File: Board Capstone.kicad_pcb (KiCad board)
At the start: 2 copper layers, 128 x 50 mm, 40 parts, among them IC201 LM2678SX-5.0, J101 Power, J102 Conn_JetsonNano, J103 Status_LED, J104 Warning_LED, J401 Haptics_1, J402 Haptics_2, SW101 SW_Pairing, U101 SN74LV1T125DBV, U102 SN74LV1T125DBV, U301 ICM-20948, U302 PCA9306, U303 TLV740P, U401 PCA9540BD_112, U402 DRV2605LDGS, U403 DRV2605LDGS

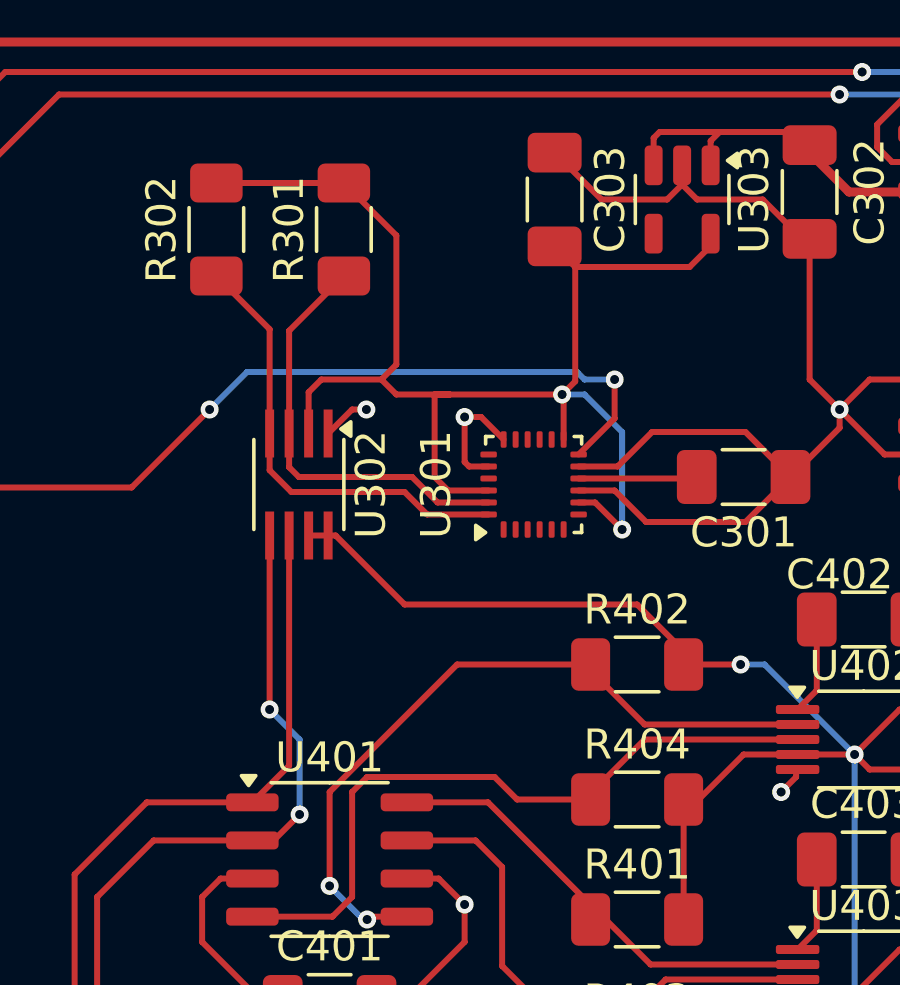
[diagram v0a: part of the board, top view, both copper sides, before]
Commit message: rev 1.1 change footprint
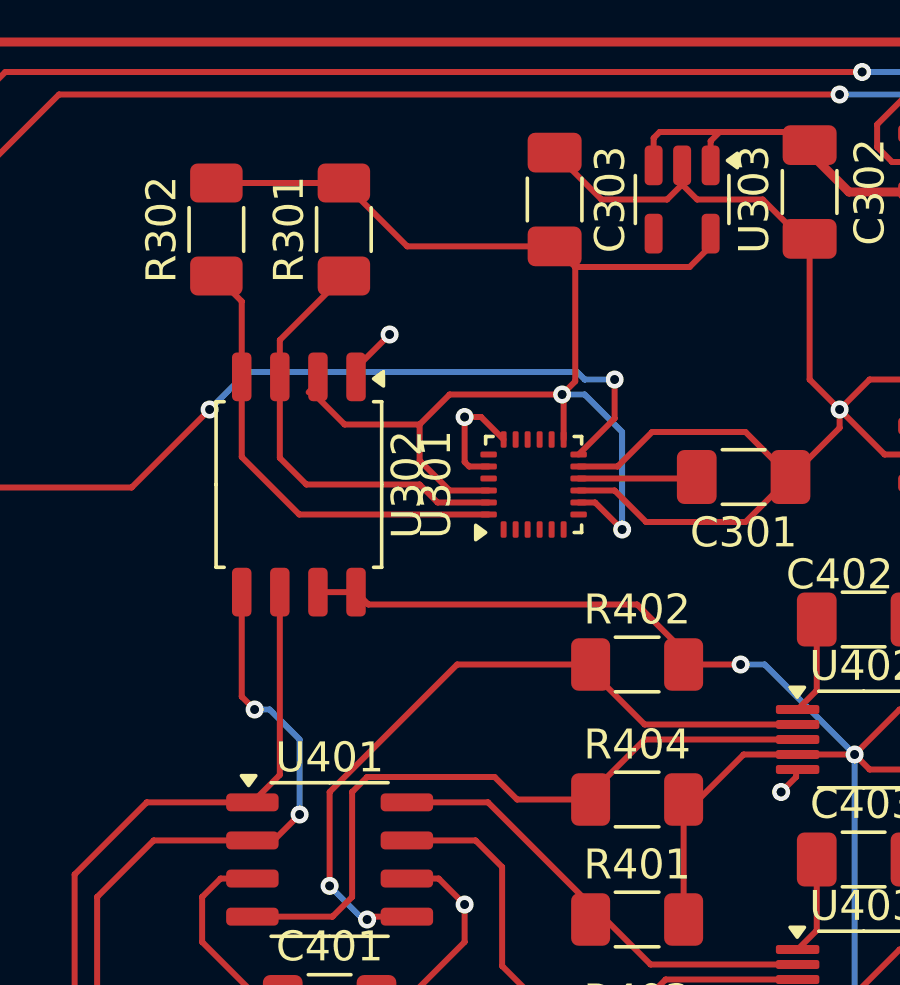
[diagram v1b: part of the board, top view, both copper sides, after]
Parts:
- U302: footprint Package_SO:SSOP-8_2.95x2.8mm_P0.65mm -> Package_SO:SOIC-8_5.3x5.3mm_P1.27mm
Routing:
- net /I2C_SLC: track 74.5 -> 72.5 mm
- net /I2C_SDA: track 80.5 -> 79.3 mm
- net +3.3V: track 163.3 -> 162.2 mm
- net IMU_VDDIO: track 47.3 -> 46.4 mm

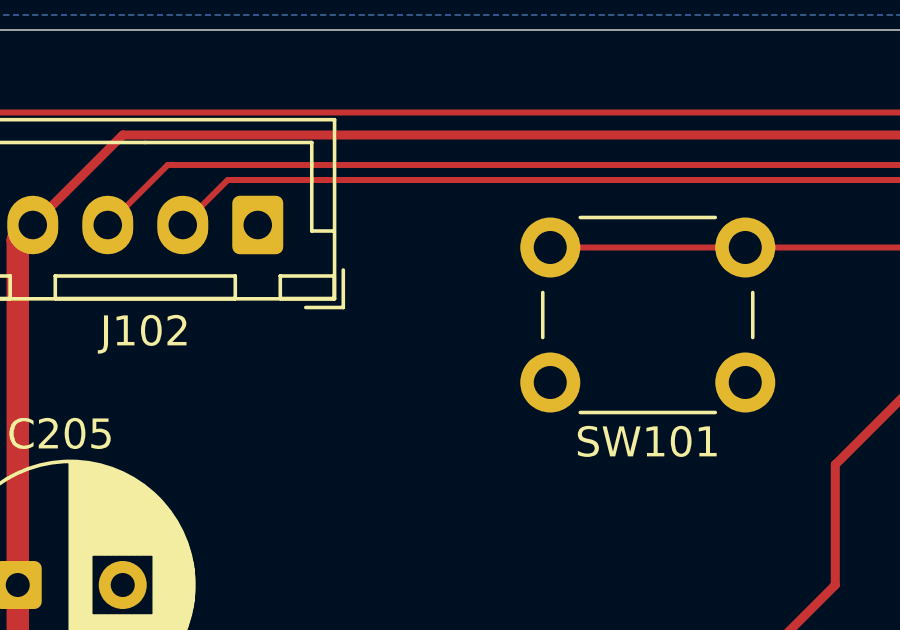
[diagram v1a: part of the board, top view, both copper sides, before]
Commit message: rev 1.1.1 Added decoupling cap to push button
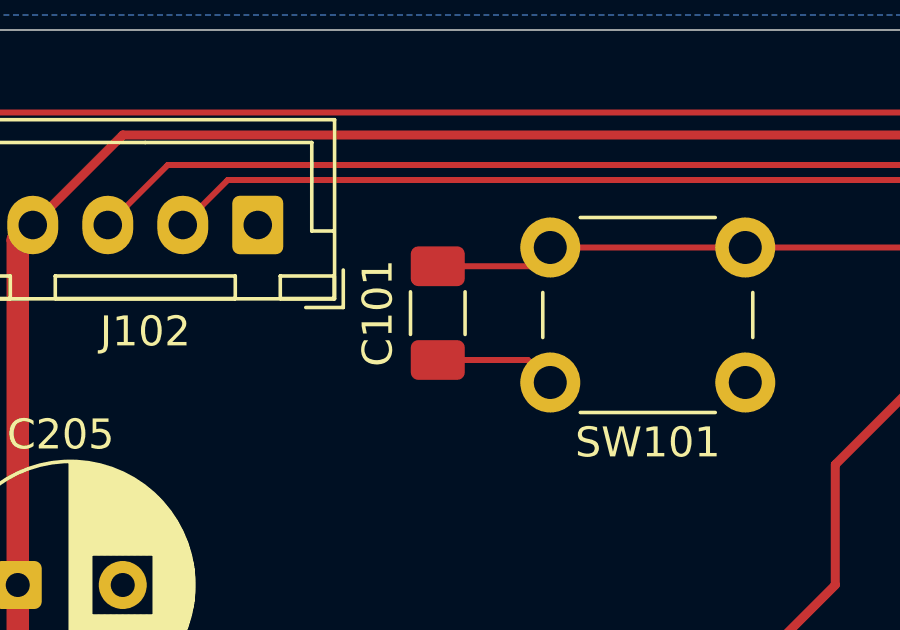
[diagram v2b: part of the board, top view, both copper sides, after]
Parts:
- added C101: 0.1uF, Capacitor_SMD:C_1206_3216Metric_Pad1.33x1.80mm_HandSolder, F.Cu at (99.0, 58.9)
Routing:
- net GND: track 113.0 -> 117.6 mm
- net Net-(A101-D13/SCK): track 14.1 -> 18.6 mm
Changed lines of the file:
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@@
 		)
 	)
+	(footprint "Capacitor_SMD:C_1206_3216Metric_Pad1.33x1.80mm_HandSolder"
+		(layer "F.Cu")
+		(at 99 58.9375 -90)
+		(descr "Capacitor SMD 1206 (3216 Metric), square (rectangular) end terminal, IPC-7351 nominal with elongated pad for handsoldering. (Body size source: IPC-SM-782 page 76, https://www.pcb-3d.com/wordpress/wp-content/uploads/ipc-sm-782a_amendment_1_and_2.pdf), generated with kicad-footprint-generator")
+		(tags "capacitor handsolder")
+		(property "Reference" "C101"
+			(at 0 2 90)
+			(layer "F.SilkS")
+			(effects
+				(font
+					(size 1 1)
+					(thickness 0.15)
+				)
+			)
+		)
+		(property "Value" "0.1uF"
+			(at 0 1.85 90)
+			(layer "F.Fab")
+			(effects
+				(font
+					(size 1 1)
+					(thickness 0.15)
+				)
+			)
+		)
+		(property "Datasheet" ""
+			(at 0 0 90)
+			(layer "F.Fab")
+			(hide yes)
+			(effects
+				(font
+					(size 1.27 1.27)
+					(thickness 0.15)
+				)
+			)
+		)
+		(property "Description" "Unpolarized capacitor, small symbol"
+			(at 0 0 90)
+			(layer "F.Fab")
+			(hide yes)
+			(effects
+				(font
+					(size 1.27 1.27)
+					(thickness 0.15)
+				)
+			)
+		)
+		(property ki_fp_filters "C_*")
+		(sheetname "/")
+		(sheetfile "Board Capstone.kicad_sch")
+		(attr smd)
+		(fp_line
+			(start -0.711252 0.91)
+			(end 0.711252 0.91)
+			(stroke
+				(width 0.12)
+				(type solid)
+			)
+			(layer "F.SilkS")
+		)
+		(fp_line
+			(start -0.711252 -0.91)
+			(end 0.711252 -0.91)
+			(stroke
+				(width 0.12)
+				(type solid)
+			)
+			(layer "F.SilkS")
+		)
+		(fp_line
+			(start -2.48 1.15)
+			(end -2.48 -1.15)
+			(stroke
+				(width 0.05)
+				(type solid)
+			)
+			(layer "F.CrtYd")
+		)
+		(fp_line
+			(start 2.48 1.15)
+			(end -2.48 1.15)
+			(stroke
+				(width 0.05)
+				(type solid)
+			)
+			(layer "F.CrtYd")
+		)
+		(fp_line
+			(start -2.48 -1.15)
+			(end 2.48 -1.15)
+			(stroke
+				(width 0.05)
+				(type solid)
+			)
+			(layer "F.CrtYd")
+		)
+		(fp_line
+			(start 2.48 -1.15)
+			(end 2.48 1.15)
+			(stroke
+				(width 0.05)
+				(type solid)
+			)
+			(layer "F.CrtYd")
+		)
+		(fp_line
+			(start -1.6 0.8)
+			(end -1.6 -0.8)
+			(stroke
+				(width 0.1)
+				(type solid)
+			)
+			(layer "F.Fab")
+		)
+		(fp_line
+			(start 1.6 0.8)
+			(end -1.6 0.8)
+			(stroke
+				(width 0.1)
+				(type solid)
+			)
+			(layer "F.Fab")
+		)
+		(fp_line
+			(start -1.6 -0.8)
+			(end 1.6 -0.8)
+			(stroke
+				(width 0.1)
+				(type solid)
+			)
+			(layer "F.Fab")
+		)
+		(fp_line
+			(start 1.6 -0.8)
+			(end 1.6 0.8)
+			(stroke
+				(width 0.1)
+				(type solid)
+			)
+			(layer "F.Fab")
+		)
+		(fp_text user "${REFERENCE}"
+			(at 0 0 90)
+			(layer "F.Fab")
+			(effects
+				(font
+					(size 0.8 0.8)
+					(thickness 0.12)
+				)
+			)
+		)
+		(pad "1" smd roundrect
+			(at -1.5625 0 270)
+			(size 1.325 1.8)
+			(layers "F.Cu" "F.Mask" "F.Paste")
+			(roundrect_rratio 0.188679)
+			(net 23 "Net-(A101-D13{slash}SCK)")
+			(pintype "passive")
+		)
+		(pad "2" smd roundrect
+			(at 1.5625 0 270)
+			(size 1.325 1.8)
+			(layers "F.Cu" "F.Mask" "F.Paste")
+			(roundrect_rratio 0.188679)
+			(net 10 "GND")
+			(pintype "passive")
+		)
+		(embedded_fonts no)
+		(model "${KICAD9_3DMODEL_DIR}/Capacitor_SMD.3dshapes/C_1206_3216Metric.step"
+			(offset
+				(xyz 0 0 0)
+			)
+			(scale
+				(xyz 1 1 1)
+			)
+			(rotate
+				(xyz 0 0 0)
+			)
+		)
+	)
 	(footprint "Diode_THT:D_DO-41_SOD81_P10.16mm_Horizontal"
 		(layer "F.Cu")
@@
 	)
 	(segment
+		(start 102 60.5)
+		(end 98.5 60.5)
+		(width 0.2)
+		(layer "F.Cu")
+		(net 10)
+	)
+	(segment
 		(start 162.5 63.5)
 		(end 163.5 64.5)
@@
 	)
 	(segment
+		(start 102.75 61.25)
+		(end 102 60.5)
+		(width 0.2)
+		(layer "F.Cu")
+		(net 10)
+	)
+	(segment
 		(start 168.55 75.5)
 		(end 168.8 75.25)
@@
 	)
 	(segment
+		(start 102.125 57.375)
+		(end 98.5 57.375)
+		(width 0.2)
+		(layer "F.Cu")
+		(net 23)
+	)
+	(segment
 		(start 109.25 56.75)
 		(end 102.75 56.75)
 		(width 0.2)
 		(layer "F.Cu")
+		(net 23)
+	)
+	(segment
+		(start 102.75 56.75)
+		(end 102.125 57.375)
+		(width 0.2)
+		(layer "F.Cu")

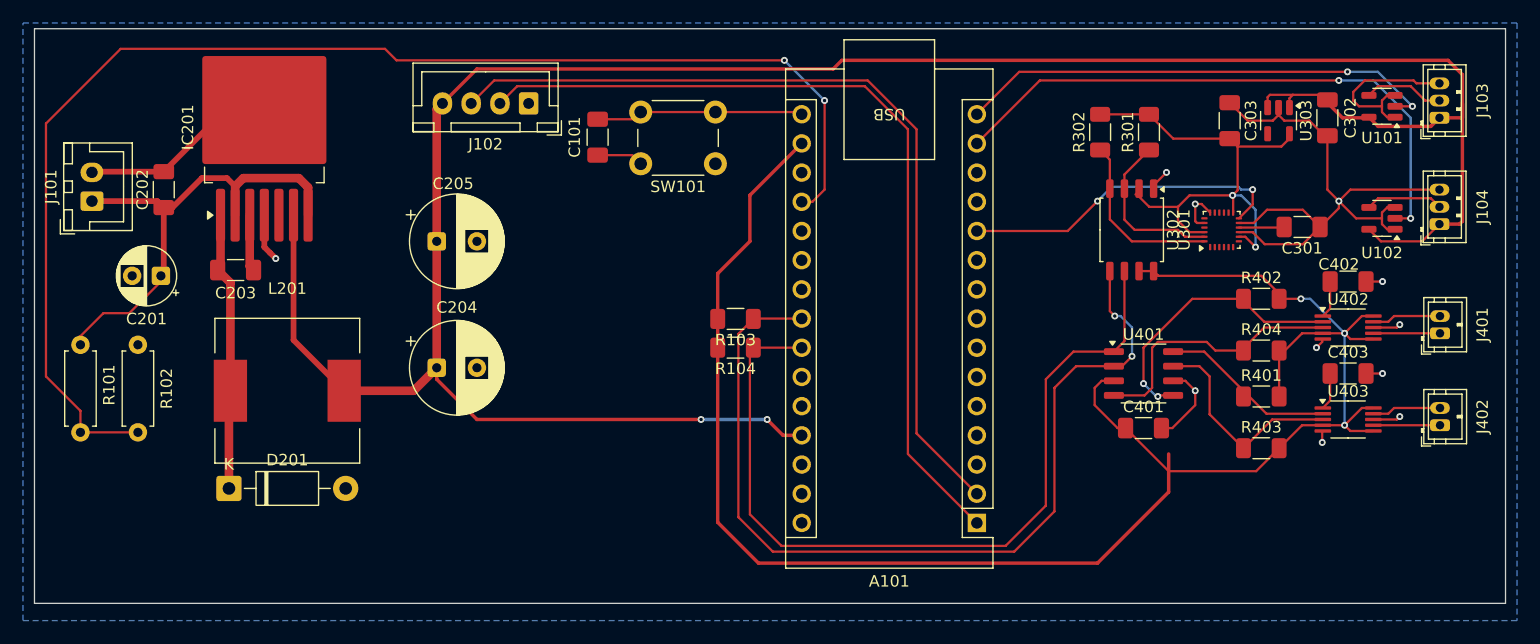
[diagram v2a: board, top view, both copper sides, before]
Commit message: Rev 1.2 Add 12v buck converter
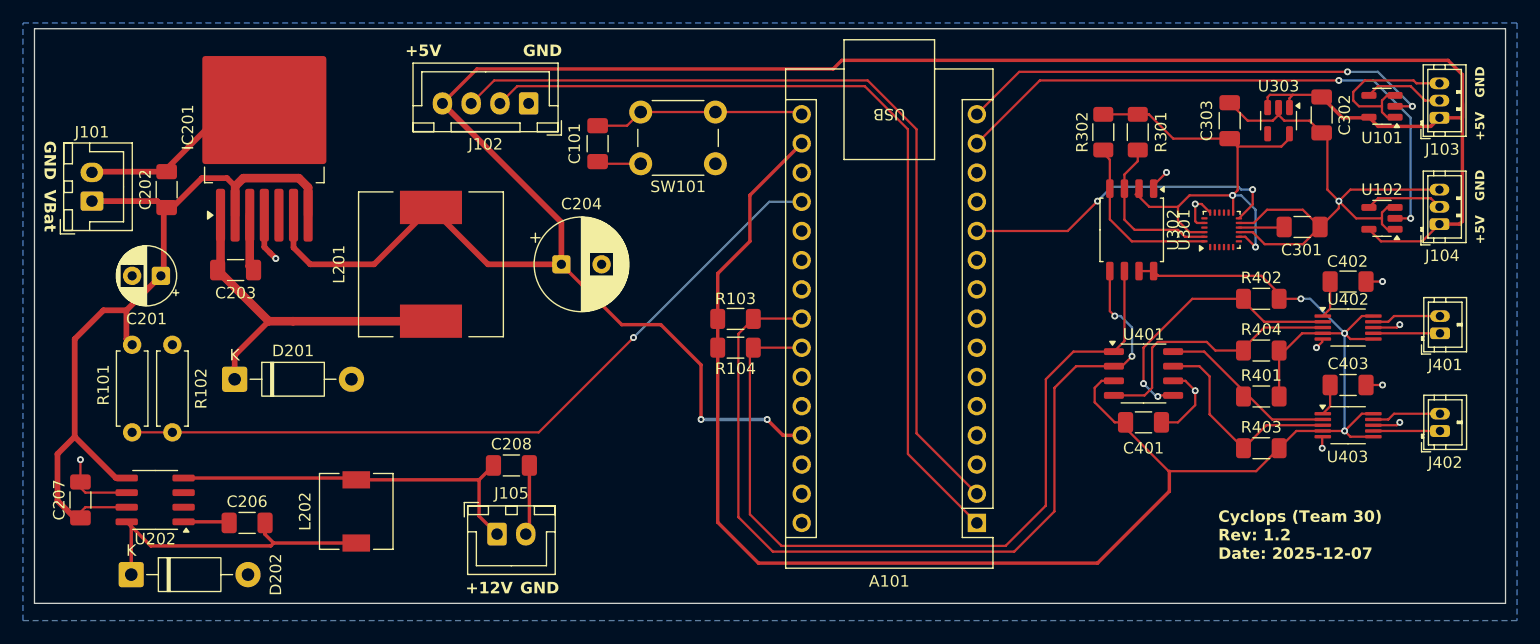
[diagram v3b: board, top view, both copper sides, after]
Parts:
- removed C205: 180uF, Capacitor_THT:CP_Radial_D8.0mm_P3.50mm
- added C206: 0.01uF, Capacitor_SMD:C_1206_3216Metric_Pad1.33x1.80mm_HandSolder, F.Cu at (68.5, 92.5)
- added C207: 1uF, Capacitor_SMD:C_1206_3216Metric_Pad1.33x1.80mm_HandSolder, F.Cu at (54.0, 90.5)
- added C208: 47uF, Capacitor_SMD:C_1206_3216Metric_Pad1.33x1.80mm_HandSolder, F.Cu at (91.5, 87.5)
- added D202: ~, Diode_THT:D_DO-41_SOD81_P10.16mm_Horizontal, F.Cu at (58.4, 97.0)
- added J105: Lidar Power, Connector_JST:JST_XH_B2B-XH-A_1x02_P2.50mm_Vertical, F.Cu at (90.2, 93.5)
- added L202: 22uH, Inductor_SMD:L_6.3x6.3_H3, F.Cu at (78.0, 91.5)
- added U202: LM2675M-12, Package_SO:SOIC-8_3.9x4.9mm_P1.27mm, F.Cu at (60.5, 90.5)
- moved L201 16.7 mm to (84.5, 70.0), turned to 90 degrees
- moved C204 14.1 mm to (95.8, 70.0)
- moved D201 9.51 mm to (67.4, 80.0)
- moved R101 4.50 mm to (58.5, 77.0)
- moved R102 3.00 mm to (62.0, 84.6)
- moved C403 1.00 mm to (164.3, 80.5)
- moved R301 0.97 mm to (146.0, 58.5)
- moved C101 0.56 mm to (99.0, 59.5)
- moved C302 0.56 mm to (162.0, 57.0)
- moved C401 0.50 mm to (146.5, 83.8)
- moved J402 0.50 mm to (172.3, 84.5)
- moved U403 0.50 mm to (164.3, 84.0)
- moved R302 0.28 mm to (143.0, 58.5)
- moved C202 0.25 mm to (61.5, 63.5)
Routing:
- net /V_BATT: track 115.6 -> 66.6 mm, vias 2 -> 1
- net +12V: track 0.00 -> 32.9 mm
- net +BATT: track 42.2 -> 74.0 mm
- net Net-(D202-K): track 0.00 -> 27.8 mm
- net GND: track 117.6 -> 130.2 mm, vias 11 -> 12
- net Net-(D201-K): track 24.6 -> 31.6 mm
- net +5V: track 218.8 -> 213.8 mm
- net Net-(U202-CB): track 0.00 -> 4.00 mm
- net +3.3V: track 162.2 -> 161.2 mm
- net Net-(U403-REG): track 3.26 -> 2.76 mm
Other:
- board text added: "+12V"
- board text added: "+5V"
- board text added: "Cyclops (Team 30) Rev: 1.2 Date: 2025-12-07"
- board text added: "GND"
- board text added: "VBat"
